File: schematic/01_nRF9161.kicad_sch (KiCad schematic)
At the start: 1 part, among them U1 NRF9161-LACA-R7

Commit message: Schematic: add C40 100nF X7R on SIM_1V8 at U1; D3-D7 values restored (Function field); D7 DNP; ERC 0 errors
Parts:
- added C40: 100nF, Capacitor_SMD:C_0402_1005Metric, symbol Device:C
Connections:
- net GND: now also C40.2
- net SIM_1V8: now also C40.1
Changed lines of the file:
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@@
+		)
+	)
+	(symbol
+		(lib_id "Device:C")
+		(at 45.72 237.49 0)
+		(unit 1)
+		(exclude_from_sim no)
+		(in_bom yes)
+		(on_board yes)
+		(dnp no)
+		(property "Reference" "C40"
+			(at 46.99 236.22 0)
+			(show_name no)
+			(do_not_autoplace no)
+			(effects
+				(font
+					(size 1.27 1.27)
+				)
+				(justify left)
+			)
+		)
+		(property "Value" "100nF"
+			(at 46.99 238.76000000000002 0)
+			(show_name no)
+			(do_not_autoplace no)
+			(effects
+				(font
+					(size 1.27 1.27)
+				)
+				(justify left)
+			)
+		)
+		(property "Footprint" "Capacitor_SMD:C_0402_1005Metric"
+			(at 46.685 233.68 0)
+			(hide yes)
+			(show_name no)
+			(do_not_autoplace no)
+			(effects
+				(font
+					(size 1.27 1.27)
+				)
+			)
+		)
+		(property "Datasheet" ""
+			(at 45.72 237.49 0)
+			(hide yes)
+			(show_name no)
+			(do_not_autoplace no)
+			(effects
+				(font
+					(size 1.27 1.27)
+				)
+			)
+		)
+		(property "Description" "SIM_1V8 decoupling at modem (U1 pad 49), 100nF 10V X7R 0402"
+			(at 45.72 237.49 0)
+			(hide yes)
+			(show_name no)
+			(do_not_autoplace no)
+			(effects
+				(font
+					(size 1.27 1.27)
+				)
+			)
+		)
+		(property "Manufacturer" "Murata"
+			(at 45.72 237.49 0)
+			(hide yes)
+			(show_name no)
+			(do_not_autoplace no)
+			(effects
+				(font
+					(size 1.27 1.27)
+				)
+			)
+		)
+		(property "MPN" "GRM155R71A104KA01D"
+			(at 45.72 237.49 0)
+			(hide yes)
+			(show_name no)
+			(do_not_autoplace no)
+			(effects
+				(font
+					(size 1.27 1.27)
+				)
+			)
+		)
+		(pin "1"
+		)
+		(pin "2"
+		)
+		(instances
+			(project "nRF9161-DEV-BOARD"
+				(path "/e1caf6a7-e2a0-4ff1-8424-4d92c0348b6b/a281c411-c6a9-483c-bcd2-9828bb4a9c02"
+					(reference "C40")
+					(unit 1)
+				)
+			)
+		)
+	)
+	(global_label "SIM_1V8"
+		(at 45.72 233.68 90)
+		(effects
+			(font
+				(size 1.27 1.27)
+			)
+			(justify left)
+		)
+	)
+	(global_label "GND"
+		(at 45.72 241.3 270)
+		(effects
+			(font
+				(size 1.27 1.27)
+			)
+			(justify right)
 		)
 	)

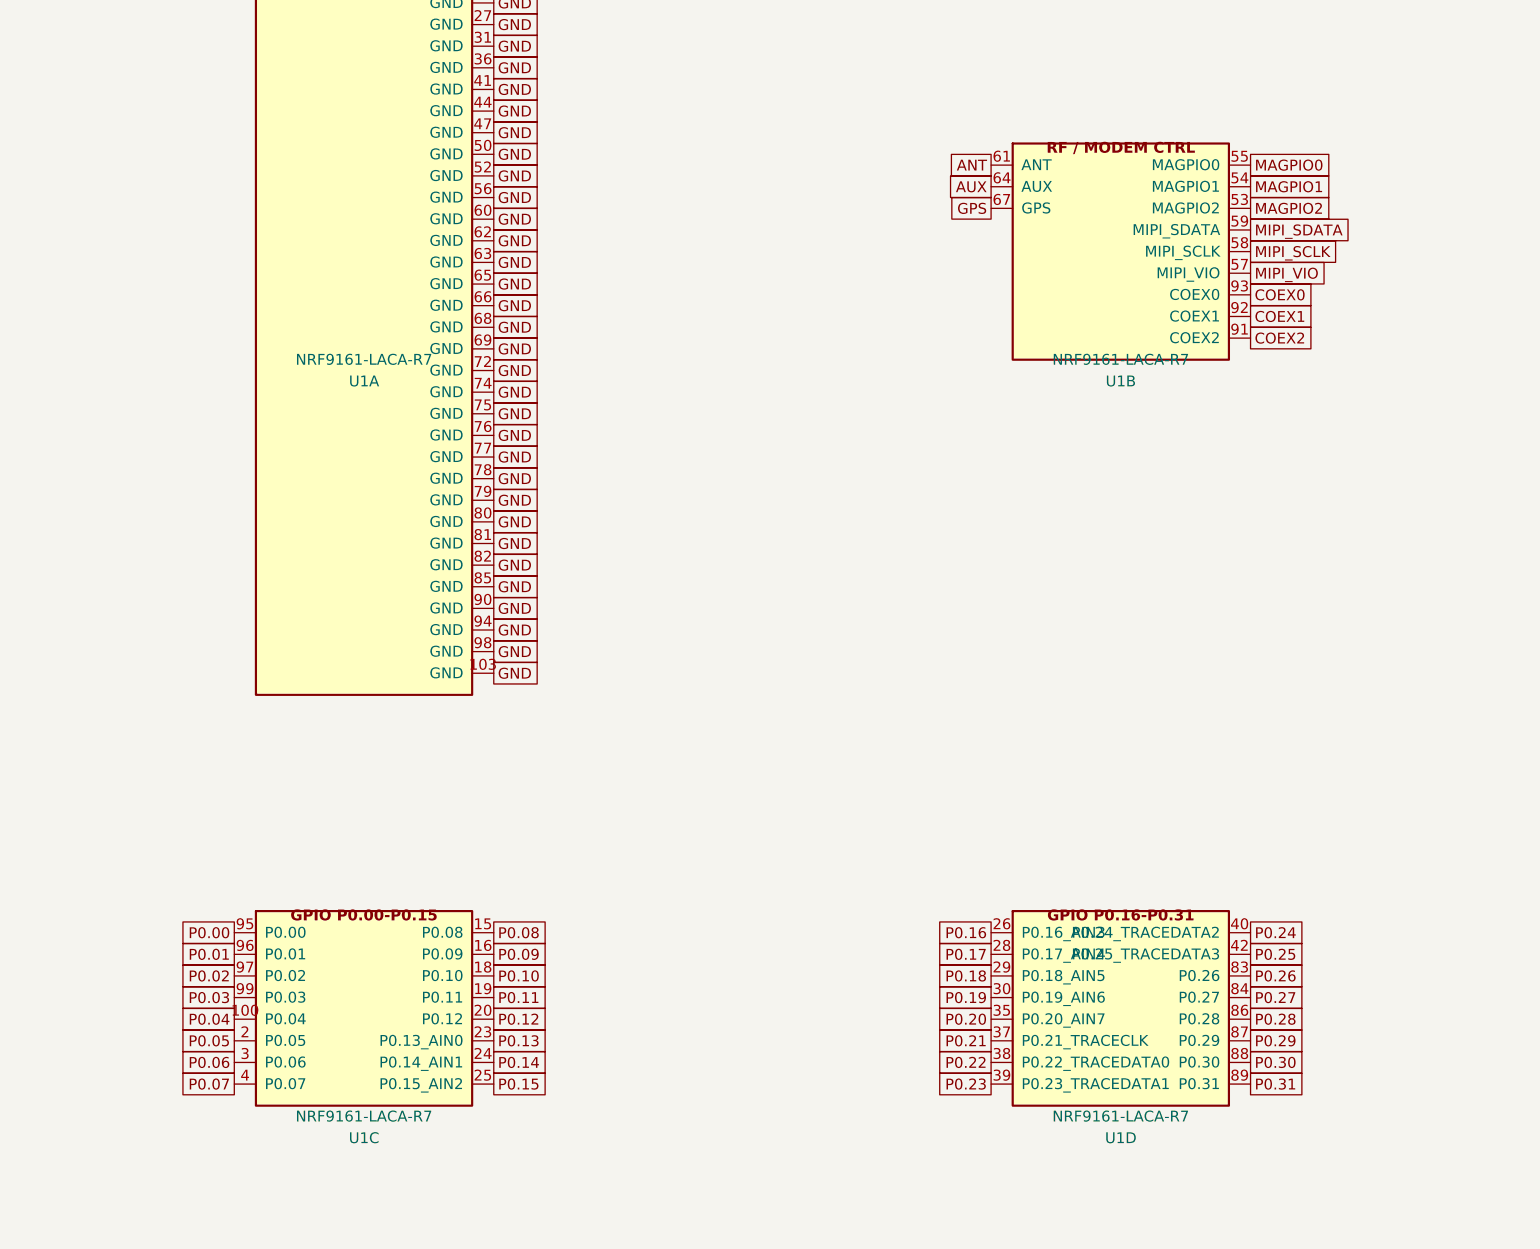
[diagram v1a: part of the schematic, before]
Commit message: v2: simplify to UART modem module (J20 host header, LXC translators); remove J1, J3, J6, J9-J18, optional parts
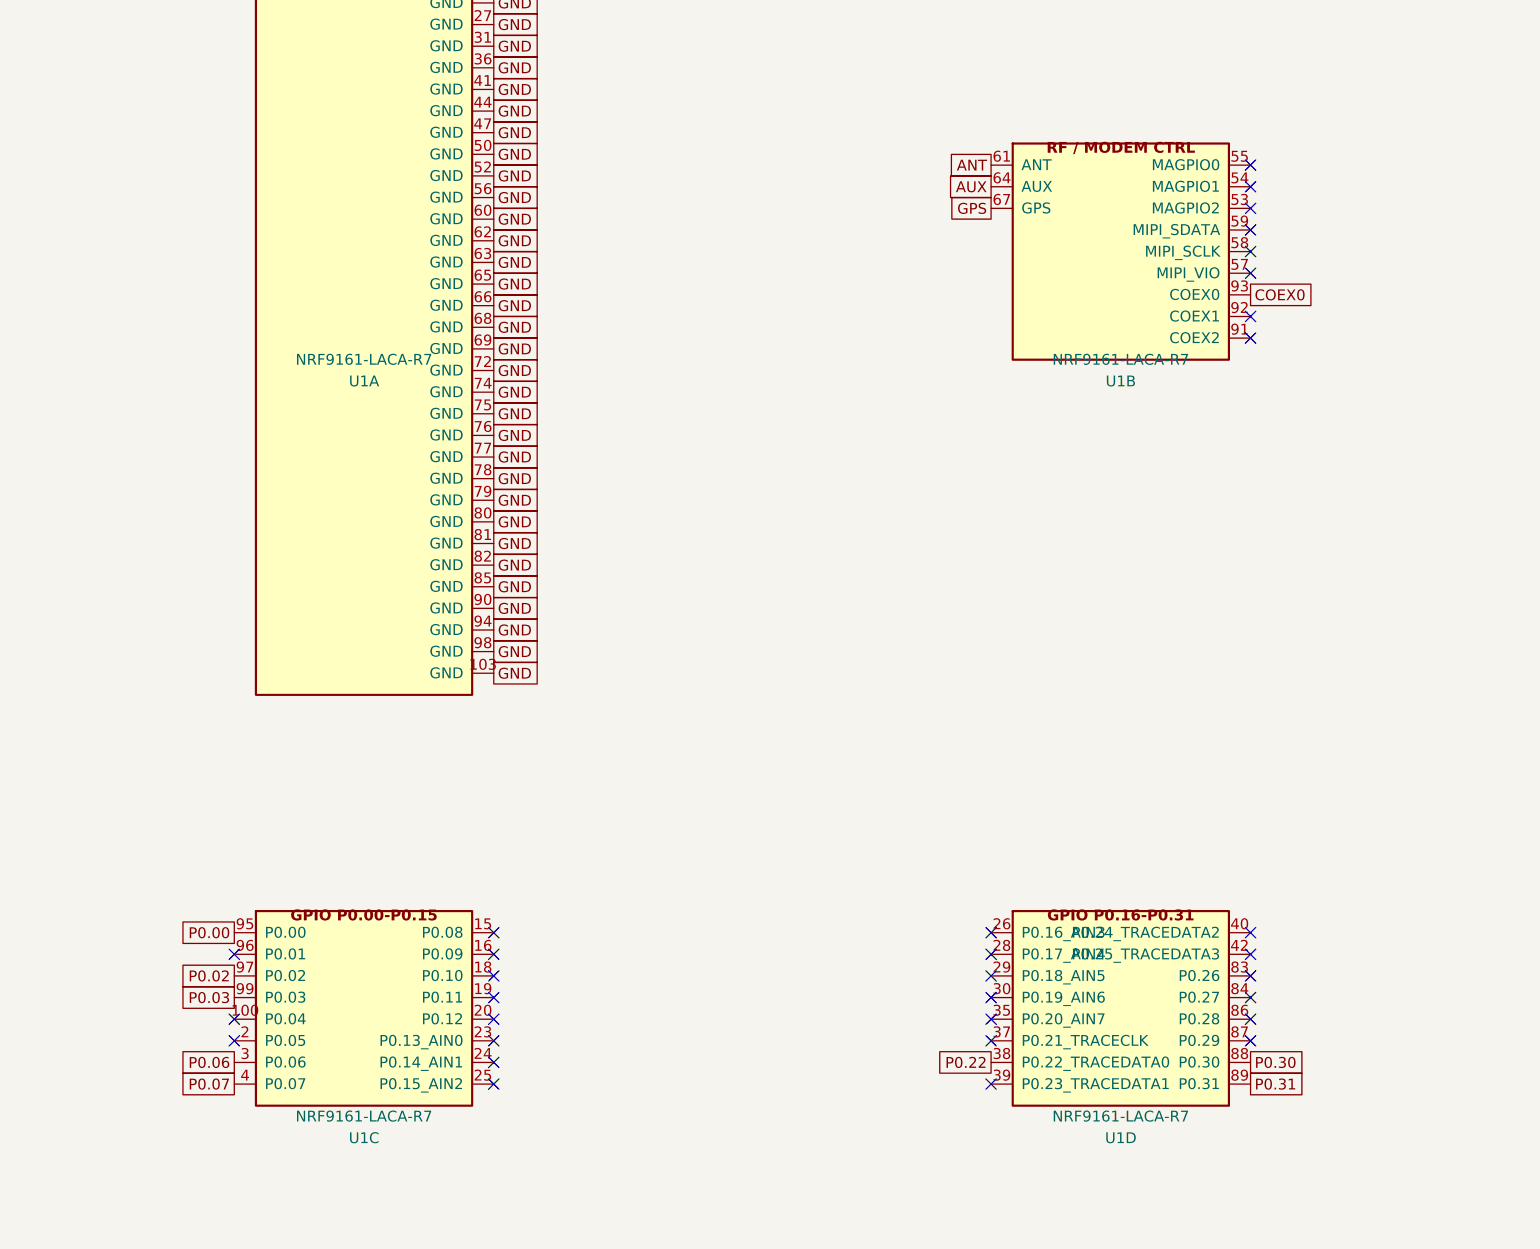
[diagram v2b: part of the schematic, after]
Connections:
- net COEX1: no longer names the net of U1.92 (COEX1)
- net COEX2: no longer names the net of U1.91 (COEX2)
- net MAGPIO0: no longer names the net of U1.55 (MAGPIO0)
- net MAGPIO1: no longer names the net of U1.54 (MAGPIO1)
- net MAGPIO2: no longer names the net of U1.53 (MAGPIO2)
- net MIPI_SCLK: no longer names the net of U1.58 (MIPI_SCLK)
- net MIPI_SDATA: no longer names the net of U1.59 (MIPI_SDATA)
- net MIPI_VIO: no longer names the net of U1.57 (MIPI_VIO)
- net P0.01: no longer names the net of U1.96 (P0.01)
- net P0.04: no longer names the net of U1.100 (P0.04)
- net P0.05: no longer names the net of U1.2 (P0.05)
- net P0.08: no longer names the net of U1.15 (P0.08)
- net P0.09: no longer names the net of U1.16 (P0.09)
- net P0.10: no longer names the net of U1.18 (P0.10)
- net P0.11: no longer names the net of U1.19 (P0.11)
- net P0.12: no longer names the net of U1.20 (P0.12)
- net P0.13: no longer names the net of U1.23 (P0.13_AIN0)
- net P0.14: no longer names the net of U1.24 (P0.14_AIN1)
- net P0.15: no longer names the net of U1.25 (P0.15_AIN2)
- net P0.16: no longer names the net of U1.26 (P0.16_AIN3)
- net P0.17: no longer names the net of U1.28 (P0.17_AIN4)
- net P0.18: no longer names the net of U1.29 (P0.18_AIN5)
- net P0.19: no longer names the net of U1.30 (P0.19_AIN6)
- net P0.20: no longer names the net of U1.35 (P0.20_AIN7)
- net P0.21: no longer names the net of U1.37 (P0.21_TRACECLK)
- net P0.23: no longer names the net of U1.39 (P0.23_TRACEDATA1)
- net P0.24: no longer names the net of U1.40 (P0.24_TRACEDATA2)
- net P0.25: no longer names the net of U1.42 (P0.25_TRACEDATA3)
- net P0.26: no longer names the net of U1.83 (P0.26)
- net P0.27: no longer names the net of U1.84 (P0.27)
- net P0.28: no longer names the net of U1.86 (P0.28)
- net P0.29: no longer names the net of U1.87 (P0.29)
- no-connect marks 30 -> 62

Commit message: v2 BOM: apply footprint-consistent MPNs + LCSC IDs, JLC BOM, audit reports (U4 footprint pending Layout)
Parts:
- C40: LCSC (none) -> C71687
- U1: LCSC (none) -> C21547412; MPN (none) -> NRF9161-LACA-R7; Manufacturer (none) -> Nordic Semiconductor
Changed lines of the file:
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@@
+			)
+		)
+		(property "MPN" "NRF9161-LACA-R7"
+			(at 88.9 88.9 0)
+			(hide yes)
+			(effects
+				(font
+					(size 1.27 1.27)
+				)
+			)
+		)
+		(property "LCSC" "C21547412"
+			(at 88.9 88.9 0)
+			(hide yes)
+			(effects
+				(font
+					(size 1.27 1.27)
+				)
+			)
+		)
+		(property "Manufacturer" "Nordic Semiconductor"
+			(at 88.9 88.9 0)
+			(hide yes)
+			(effects
+				(font
+					(size 1.27 1.27)
+				)
 			)
 		)
@@
 			)
 		)
+		(property "MPN" "NRF9161-LACA-R7"
+			(at 177.8 88.9 0)
+			(hide yes)
+			(effects
+				(font
+					(size 1.27 1.27)
+				)
+			)
+		)
+		(property "LCSC" "C21547412"
+			(at 177.8 88.9 0)
+			(hide yes)
+			(effects
+				(font
+					(size 1.27 1.27)
+				)
+			)
+		)
+		(property "Manufacturer" "Nordic Semiconductor"
+			(at 177.8 88.9 0)
+			(hide yes)
+			(effects
+				(font
+					(size 1.27 1.27)
+				)
+			)
+		)
 		(pin "53"
 		)
@@
 			)
 		)
+		(property "MPN" "NRF9161-LACA-R7"
+			(at 88.9 177.8 0)
+			(hide yes)
+			(effects
+				(font
+					(size 1.27 1.27)
+				)
+			)
+		)
+		(property "LCSC" "C21547412"
+			(at 88.9 177.8 0)
+			(hide yes)
+			(effects
+				(font
+					(size 1.27 1.27)
+				)
+			)
+		)
+		(property "Manufacturer" "Nordic Semiconductor"
+			(at 88.9 177.8 0)
+			(hide yes)
+			(effects
+				(font
+					(size 1.27 1.27)
+				)
+			)
+		)
 		(pin "100"
 		)
@@
 			)
 		)
+		(property "MPN" "NRF9161-LACA-R7"
+			(at 177.8 177.8 0)
+			(hide yes)
+			(effects
+				(font
+					(size 1.27 1.27)
+				)
+			)
+		)
+		(property "LCSC" "C21547412"
+			(at 177.8 177.8 0)
+			(hide yes)
+			(effects
+				(font
+					(size 1.27 1.27)
+				)
+			)
+		)
+		(property "Manufacturer" "Nordic Semiconductor"
+			(at 177.8 177.8 0)
+			(hide yes)
+			(effects
+				(font
+					(size 1.27 1.27)
+				)
+			)
+		)
 		(pin "26"
 		)
@@
 			)
 		)
+		(property "MPN" "NRF9161-LACA-R7"
+			(at 88.9 254 0)
+			(hide yes)
+			(effects
+				(font
+					(size 1.27 1.27)
+				)
+			)
+		)
+		(property "LCSC" "C21547412"
+			(at 88.9 254 0)
+			(hide yes)
+			(effects
+				(font
+					(size 1.27 1.27)
+				)
+			)
+		)
+		(property "Manufacturer" "Nordic Semiconductor"
+			(at 88.9 254 0)
+			(hide yes)
+			(effects
+				(font
+					(size 1.27 1.27)
+				)
+			)
+		)
 		(pin "10"
 		)
@@
 			(effects
 				(font
+					(size 1.27 1.27)
+				)
+			)
+		)
+		(property "LCSC" "C71687"
+			(at 45.72 237.49 0)
+			(hide yes)
+			(effects
+				(font
